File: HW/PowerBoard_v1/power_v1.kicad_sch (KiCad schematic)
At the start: 3 parts, among them J2 Conn_01x05, U1 MCP9700AT-ETT

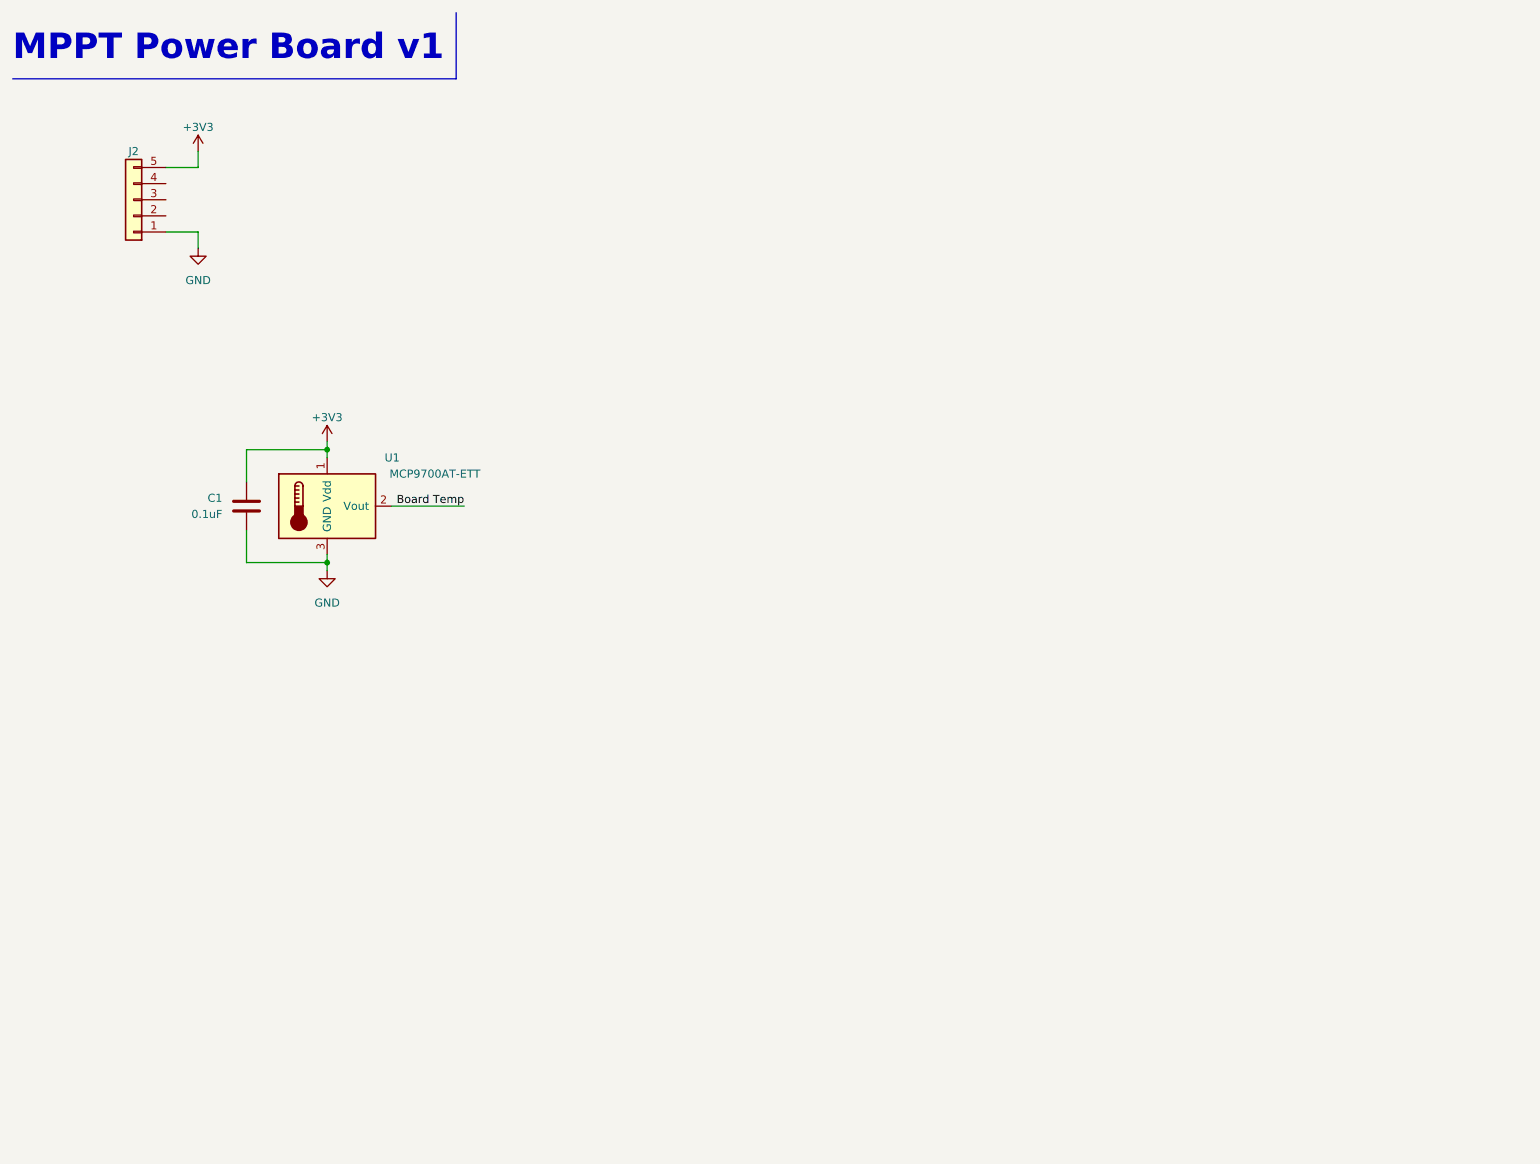
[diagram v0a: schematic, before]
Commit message: boost added to power board
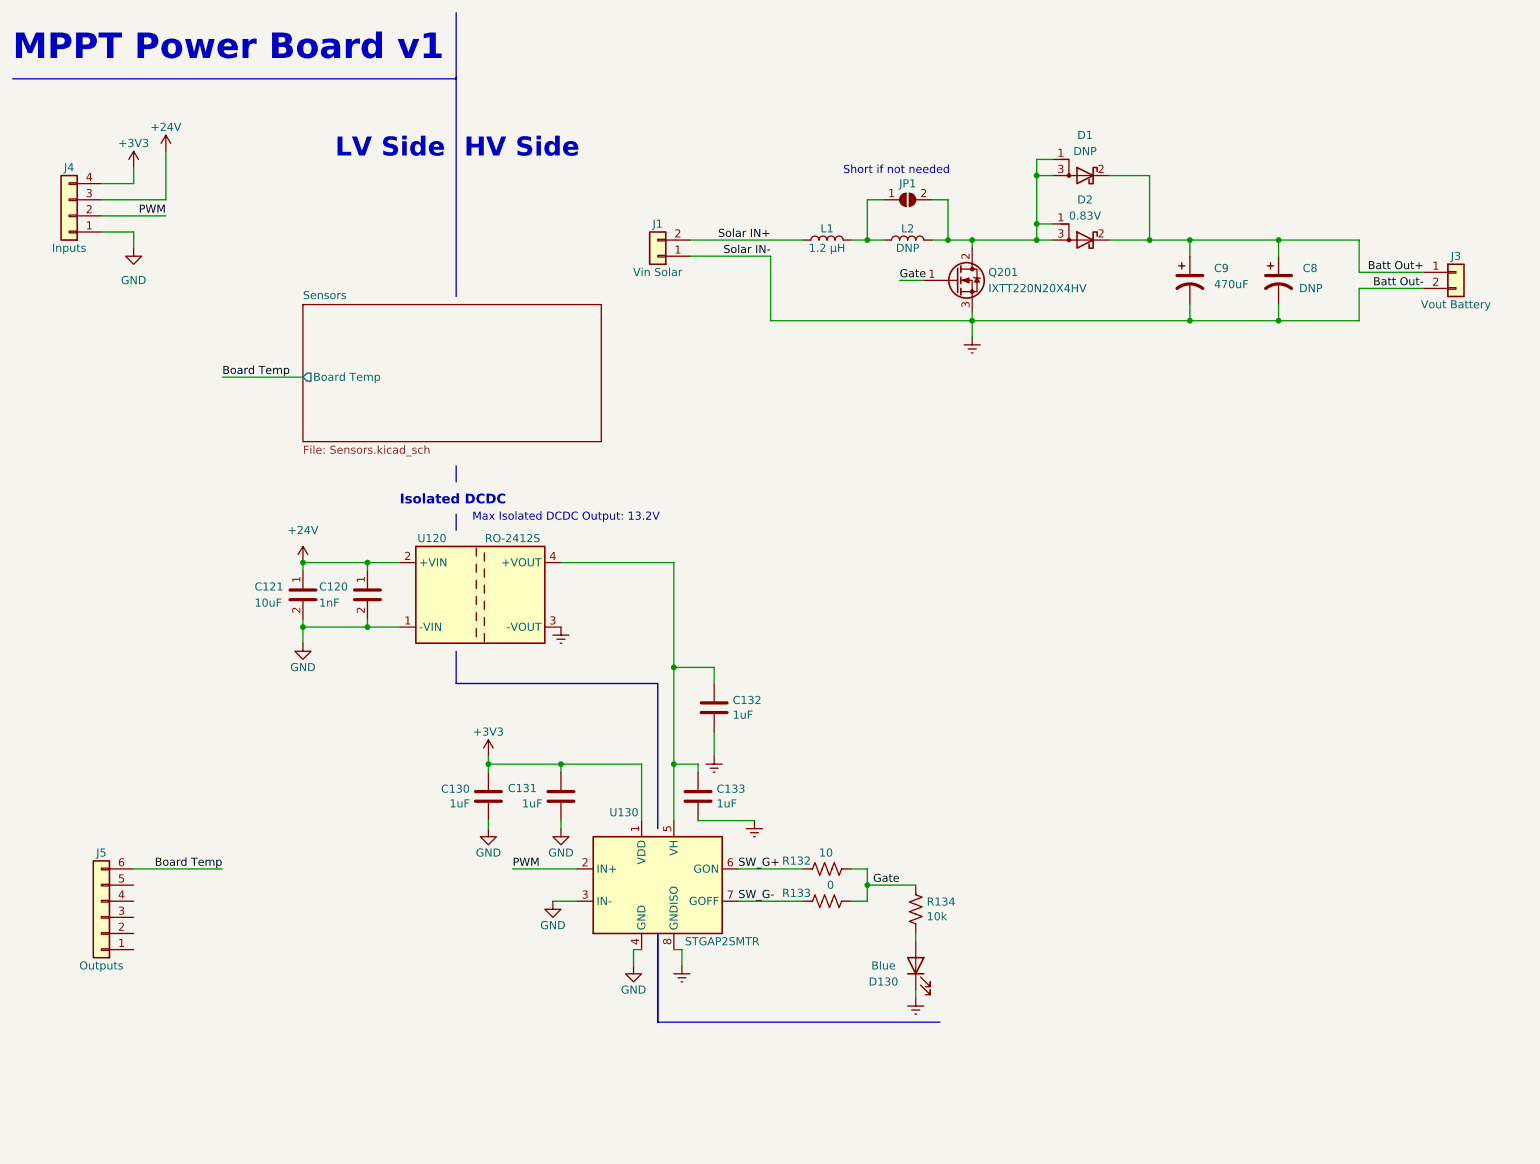
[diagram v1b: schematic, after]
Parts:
- removed C1: 0.1uF, Capacitor_SMD:C_0603_1608Metric_Pad1.08x0.95mm_HandSolder, symbol device:C
- removed J2: Conn_01x05, Connector_Molex:Molex_Micro-Fit_3.0_43650-0500_1x05_P3.00mm_Horizontal, symbol Connector_Generic:Conn_01x05
- removed U1: MCP9700AT-ETT, Package_TO_SOT_SMD:SOT-23, symbol Sensor_Temperature:MCP9700AT-ETT
- added C120: 1nF, Capacitor_SMD:C_0603_1608Metric_Pad1.08x0.95mm_HandSolder, symbol device:C
- added C121: 10uF, Capacitor_SMD:C_0603_1608Metric_Pad1.08x0.95mm_HandSolder, symbol device:C
- added C130, C131, C132, C133: 1uF, Capacitor_SMD:C_0603_1608Metric_Pad1.08x0.95mm_HandSolder, symbol device:C
- added C8, C9: 470uF, Capacitor_THT:C_Radial_D18.0mm_H35.5mm_P7.50mm, symbol device:C_Polarized_US
- added D1, D2: 0.83V, Package_TO_SOT_SMD:TO-252-2, symbol Device:D_Schottky_AKA
- added D130: Blue, LED_SMD:LED_0603_1608Metric_Pad1.05x0.95mm_HandSolder, symbol device:LED
- added J1: Vin Solar, layout:Anderson_Powerpole_45A_1x2_Horizontal_Bottom, symbol Connector_Generic:Conn_01x02
- added J3: Vout Battery, layout:Anderson_Powerpole_45A_1x2_Horizontal_Bottom, symbol Connector_Generic:Conn_01x02
- added J4: Inputs, Connector_Molex:Molex_Micro-Fit_3.0_43650-0400_1x04_P3.00mm_Horizontal, symbol Connector_Generic:Conn_01x04
- added J5: Outputs, Connector_Molex:Molex_Micro-Fit_3.0_43650-0600_1x06_P3.00mm_Horizontal, symbol Connector_Generic:Conn_01x06
- added JP1: SolderJumper_2_Open, Resistor_SMD:R_0603_1608Metric_Pad0.98x0.95mm_HandSolder, symbol Jumper:SolderJumper_2_Open
- added L1, L2: 1.2 μH, Inductor_SMD:L_Wuerth_HCM-1050, symbol Device:L
- added Q201: IXTT220N20X4HV, Package_TO_SOT_SMD:TO-268-2, symbol device:Q_NMOS_GDS
- added R132: 10, Resistor_SMD:R_0603_1608Metric_Pad0.98x0.95mm_HandSolder, symbol device:R_US
- added R133: 0, Resistor_SMD:R_0603_1608Metric_Pad0.98x0.95mm_HandSolder, symbol device:R_US
- added R134: 10k, Resistor_SMD:R_0603_1608Metric_Pad0.98x0.95mm_HandSolder, symbol device:R_US
- added U120: RO-2412S, Converter_DCDC:Converter_DCDC_RECOM_R-78S-0.1_THT, symbol Regulator_Switching:CRE1S0305S3C
- added U130: STGAP2SMTR, Package_SO:SOIC-8_3.9x4.9mm_P1.27mm, symbol Driver_FET:STGAP2SM
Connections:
- net +3V3: now also C130.1, C131.1, J4.4 (Pin_4), U130.1 (VDD)
- net Board Temp: now also J5.6 (Pin_6)
- net GND: now also C120.2, C121.2, C130.2, C131.2, J4.1 (Pin_1), U120.1 (-VIN), U130.3 (IN-), U130.4 (GND)
- new net: D1.1 (A), D1.3 (A), D2.1 (A), D2.3 (A), JP1.2 (B), L2.2, Q201.2 (D)
- new net: D130.2 (A), R134.2
- new net: JP1.1 (A), L1.2, L2.1
- new net: C132.1, C133.1, U120.4 (+VOUT), U130.5 (VH)
- new net +24V: C120.1, C121.1, J4.3 (Pin_3), U120.2 (+VIN)
- new net Batt Out+: C8.1, C9.1, D1.2 (K), D2.2 (K), J3.1 (Pin_1)
- new net Earth: C132.2, C133.2, C8.2, C9.2, D130.1 (K), J1.1 (Pin_1), J3.2 (Pin_2), Q201.3 (S), U120.3 (-VOUT), U130.8 (GNDISO)
- new net Gate: Q201.1 (G), R132.1, R133.1, R134.1
- new net PWM: J4.2 (Pin_2), U130.2 (IN+)
- new net SW_G+: R132.2, U130.6 (GON)
- new net SW_G-: R133.2, U130.7 (GOFF)
- new net Solar IN+: J1.2 (Pin_2), L1.1
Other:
- added sheet Sensors (Sensors.kicad_sch)
- note added: "HV Side"
- note added: "Isolated DCDC"
- note added: "LV Side"
- note added: "Max Isolated DCDC Output: 13.2V"
- note added: "Short if not needed"

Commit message: cleaned up schematic
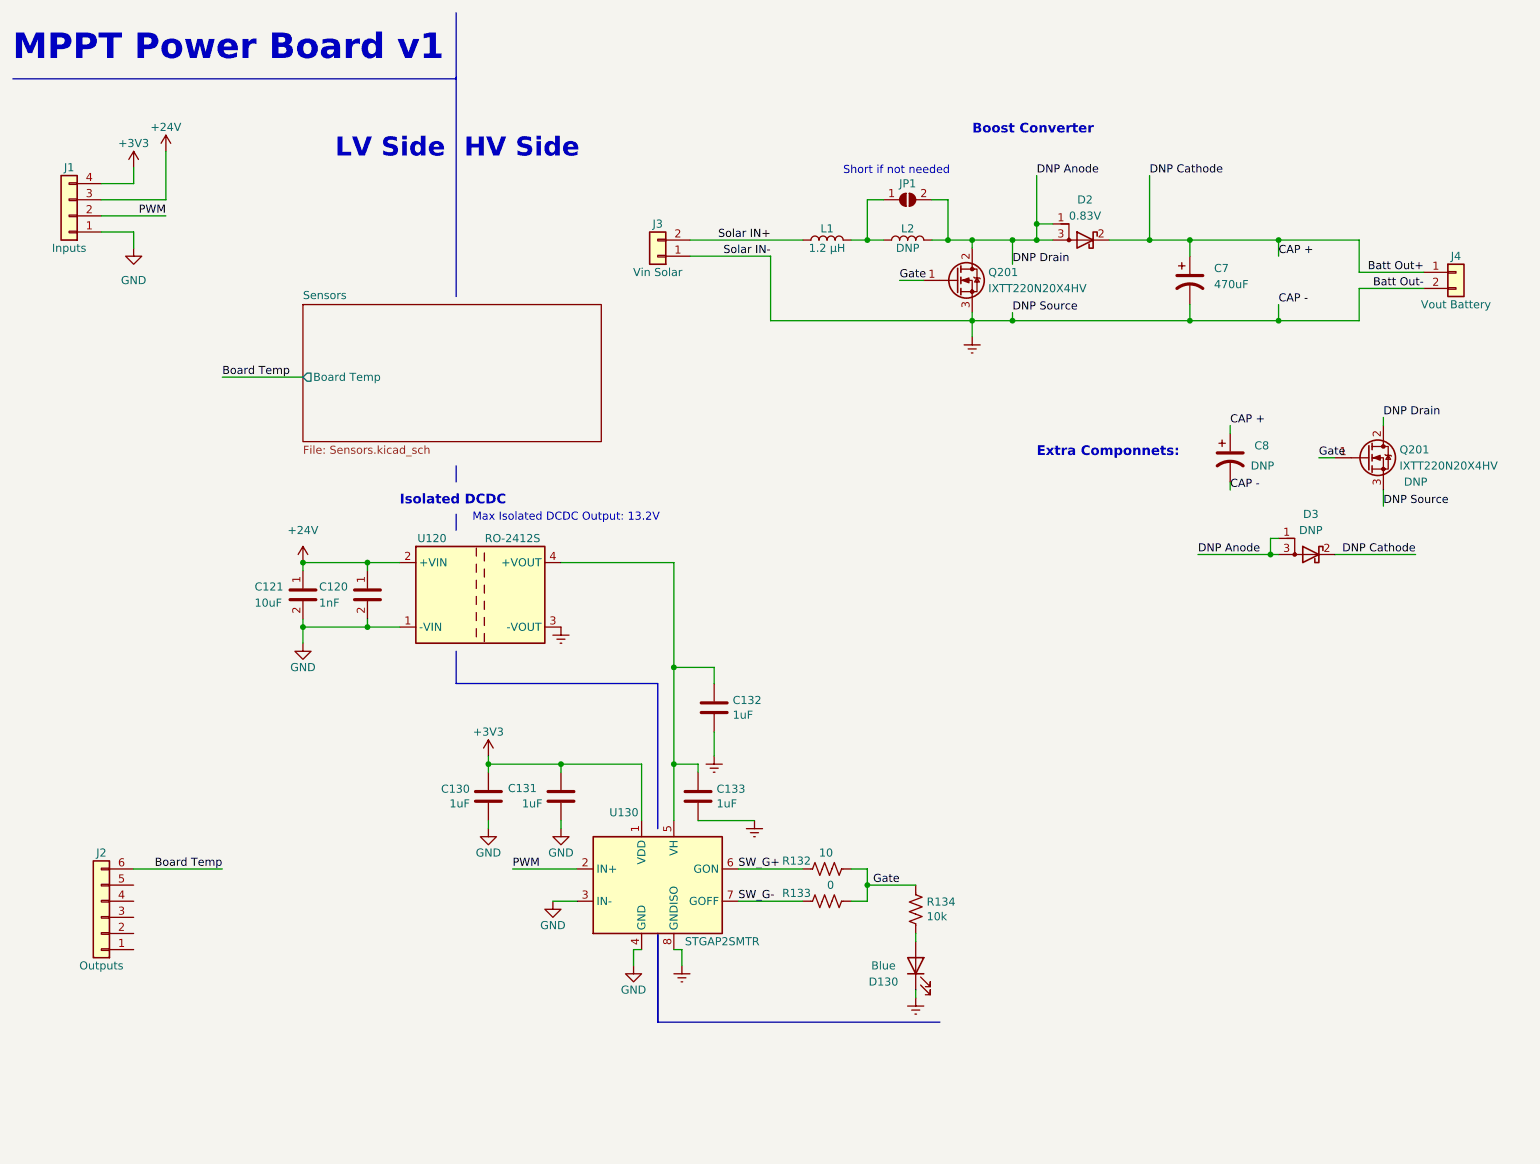
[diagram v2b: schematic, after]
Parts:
- added Q201: IXTT220N20X4HV, Package_TO_SOT_SMD:TO-268-2, symbol device:Q_NMOS_GDS
- renumbered C9 to C7, D1 to D3, J4 to J1, J5 to J2, J1 to J3, J3 to J4
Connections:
- net Earth: now also Q201.3 (S)
- net Gate: now also Q201.1 (G)
- net DNP Anode: now reaches D2.1 (A), D2.3 (A), D3.1 (A), D3.3 (A), JP1.2 (B), L2.2, Q201.2 (D)
- net DNP Anode: now also Q201.2 (D)
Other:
- note added: "Boost Converter"
- note added: "Extra Componnets:"
- moved on the sheet: D3

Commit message: update sim to simulate array better
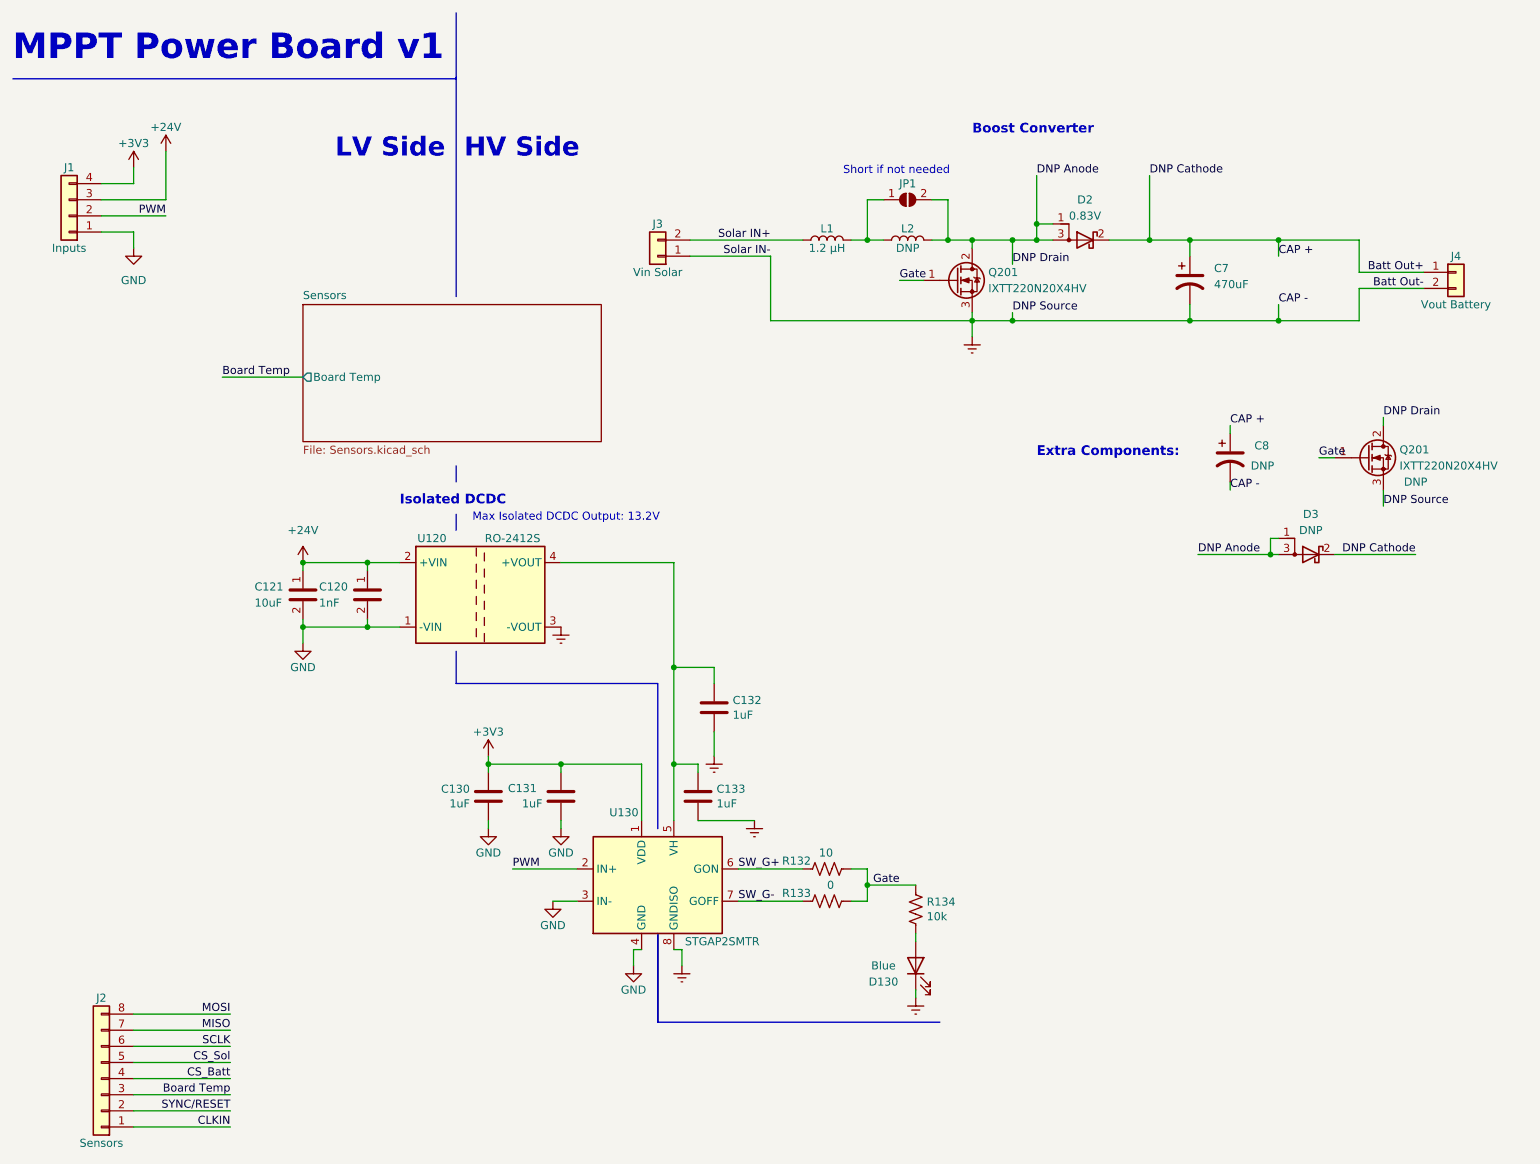
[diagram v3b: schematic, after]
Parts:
- removed J2: Outputs, Connector_Molex:Molex_Micro-Fit_3.0_43650-0600_1x06_P3.00mm_Horizontal, symbol Connector_Generic:Conn_01x06
- added J2: Sensors, Connector_Molex:Molex_Micro-Fit_3.0_43650-0800_1x08_P3.00mm_Horizontal, symbol Connector_Generic:Conn_01x08
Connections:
- net Board Temp: now also J2.3 (Pin_3)
- new net CLKIN: J2.1 (Pin_1)
- new net CS_Batt: J2.4 (Pin_4)
- new net CS_Sol: J2.5 (Pin_5)
- new net MISO: J2.7 (Pin_7)
- new net MOSI: J2.8 (Pin_8)
- new net SCLK: J2.6 (Pin_6)
- new net SYNC/RESET: J2.2 (Pin_2)
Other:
- note added: "Extra Components:"
- note removed: "Extra Componnets:"

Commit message: updates sensing
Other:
- sheet Sensors ports: added Batt IN+, Batt IN-, Solar IN+, Solar IN-; removed none
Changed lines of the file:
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@@
+    (stroke (width 0) (type default))
+  )
+  (wire (pts (xy 105.41 74.93) (xy 115.57 74.93))
     (stroke (width 0) (type default))
   )
@@
     (stroke (width 0) (type default))
   )
+  (wire (pts (xy 105.41 72.39) (xy 115.57 72.39))
+    (stroke (width 0) (type default))
+  )
   (wire (pts (xy 116.84 160.02) (xy 118.11 160.02))
     (stroke (width 0) (type default))
@@
     (stroke (width 0) (type default))
   )
+  (wire (pts (xy 105.41 62.23) (xy 115.57 62.23))
+    (stroke (width 0) (type default))
+  )
   (wire (pts (xy 204.47 77.47) (xy 204.47 78.74))
     (stroke (width 0) (type default))
@@
   )
   (wire (pts (xy 163.83 60.96) (xy 170.18 60.96))
+    (stroke (width 0) (type default))
+  )
+  (wire (pts (xy 105.41 64.77) (xy 115.57 64.77))
     (stroke (width 0) (type default))
   )
@@
     (effects (font (size 1.27 1.27)) (justify right bottom))
   )
+  (label "Solar IN+" (at 115.57 62.23 180) (fields_autoplaced)
+    (effects (font (size 1.27 1.27)) (justify right bottom))
+  )
   (label "Gate" (at 152.4 149.86 180) (fields_autoplaced)
     (effects (font (size 1.27 1.27)) (justify right bottom))
@@
     (effects (font (size 1.27 1.27)) (justify left bottom))
   )
+  (label "Batt IN+" (at 115.57 72.39 180) (fields_autoplaced)
+    (effects (font (size 1.27 1.27)) (justify right bottom))
+  )
   (label "Board Temp" (at 45.72 69.85 0) (fields_autoplaced)
     (effects (font (size 1.27 1.27)) (justify left bottom))
@@
     (effects (font (size 1.27 1.27)) (justify left bottom))
   )
+  (label "Batt IN-" (at 115.57 74.93 180) (fields_autoplaced)
+    (effects (font (size 1.27 1.27)) (justify right bottom))
+  )
   (label "PWM" (at 36.83 44.45 180) (fields_autoplaced)
     (effects (font (size 1.27 1.27)) (justify right bottom))
   )
   (label "Batt Out+" (at 234.95 53.34 180) (fields_autoplaced)
+    (effects (font (size 1.27 1.27)) (justify right bottom))
+  )
+  (label "Solar IN-" (at 115.57 64.77 180) (fields_autoplaced)
     (effects (font (size 1.27 1.27)) (justify right bottom))
   )
@@
       (effects (font (size 1.27 1.27)) (justify left))
     )
-    (instances
+    (pin "Solar IN-" input (at 105.41 64.77 0)
+      (effects (font (size 1.27 1.27)) (justify right))
+    )
+    (pin "Batt IN+" input (at 105.41 72.39 0)
+      (effects (font (size 1.27 1.27)) (justify right))
+    )
+    (pin "Solar IN+" input (at 105.41 62.23 0)
+      (effects (font (size 1.27 1.27)) (justify right))
+    )
+    (pin "Batt IN-" input (at 105.41 74.93 0)
+      (effects (font (size 1.27 1.27)) (justify right))
+    )
+    (instances

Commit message: updated sensing portion
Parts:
- removed J2: Sensors, Connector_Molex:Molex_Micro-Fit_3.0_43650-0800_1x08_P3.00mm_Horizontal, symbol Connector_Generic:Conn_01x08
- added J5: Sensors, Connector_Molex:Molex_Micro-Fit_3.0_43650-0500_1x05_P3.00mm_Horizontal, symbol Connector_Generic:Conn_01x05
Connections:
- net Board Temp: now also J5.5 (Pin_5)
- new net ADC I Batt: J5.4 (Pin_4)
- new net ADC I Sol: J5.3 (Pin_3)
- new net ADC V Batt: J5.2 (Pin_2)
- new net ADC V Sol: J5.1 (Pin_1)
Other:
- sheet Sensors ports: added ADC I Batt, ADC I Sol, ADC V Batt, ADC V Sol; removed none

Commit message: added resistors for sensing
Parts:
- added TP3: 24V, TestPoint:TestPoint_THTPad_1.0x1.0mm_Drill0.5mm, symbol Connector:TestPoint
- added TP4: GND, TestPoint:TestPoint_THTPad_1.0x1.0mm_Drill0.5mm, symbol Connector:TestPoint
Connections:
- net +24V: now also TP3.1
- net Batt Out+: no longer C7.1, C8.1, D2.2 (K), D3.2 (K)
- net GND: now also TP4.1
- net Solar IN+: no longer L1.1
- new net CAP +: C7.1, C8.1, D2.2 (K), D3.2 (K)
- new net SHUNT IN: L1.1
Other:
- sheet Sensors ports: added Batt Out+, SHUNT IN, SHUNT OUT; removed Batt IN+, Batt IN-, Solar IN-
- moved on the sheet: J3, J4
